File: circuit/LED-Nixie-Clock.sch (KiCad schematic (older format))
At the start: 37 parts, among them J1 USB Micro, J2 Debug, J3 Serial, SW1 Boot0, U1 MCP1700-3302E_SOT23, U2 STM32F103C8Tx, Y1 8MHz, Y2 32.768kHz

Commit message: Reroute PCB traces for more compact layout and 5032 crystal
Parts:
- Y1: footprint Crystal:Crystal_SMD_HC49-SD -> Crystal:Crystal_SMD_5032-2Pin_5.0x3.2mm
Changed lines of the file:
@@
 F 0 "Y1" V 1554 3981 50  0000 L CNN
 F 1 "8MHz" V 1645 3981 50  0000 L CNN
-F 2 "Crystal:Crystal_SMD_HC49-SD" H 1600 3850 50  0001 C CNN
+F 2 "Crystal:Crystal_SMD_5032-2Pin_5.0x3.2mm" H 1600 3850 50  0001 C CNN
 F 3 "~" H 1600 3850 50  0001 C CNN
 	1    1600 3850

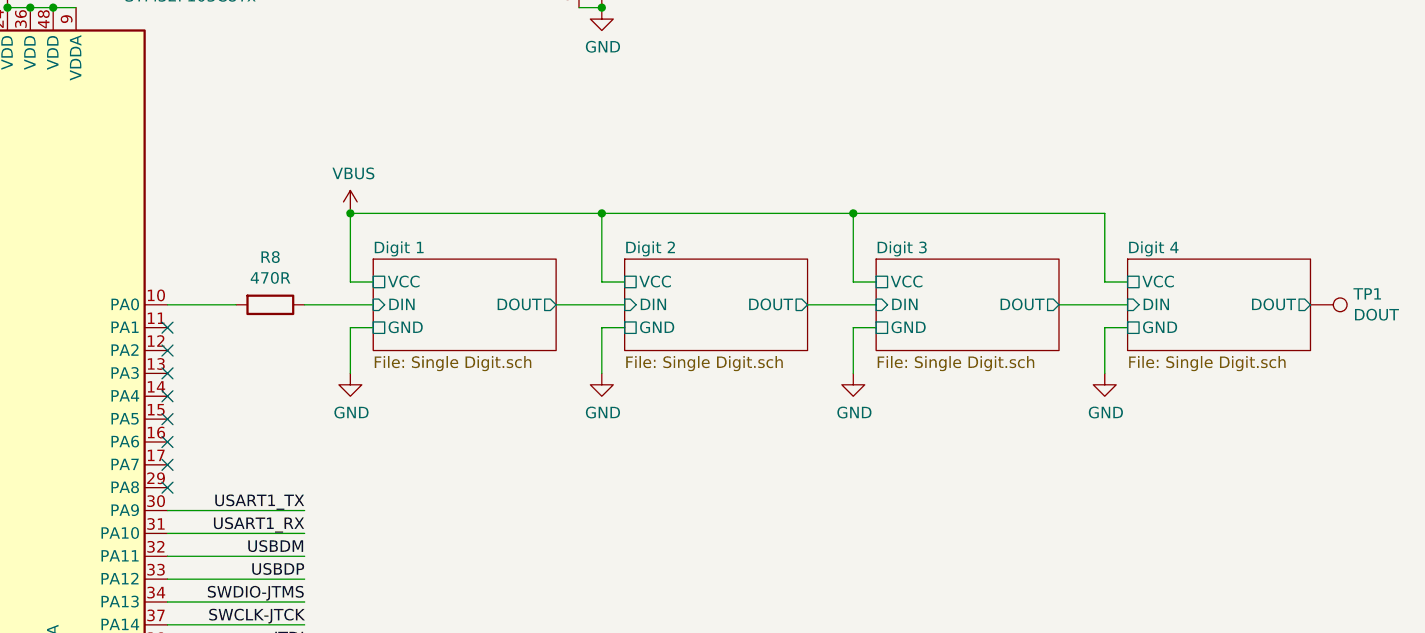
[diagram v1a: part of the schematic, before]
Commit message: Move LED data bus to PA2 (which is on the same pin as USART2 Tx)
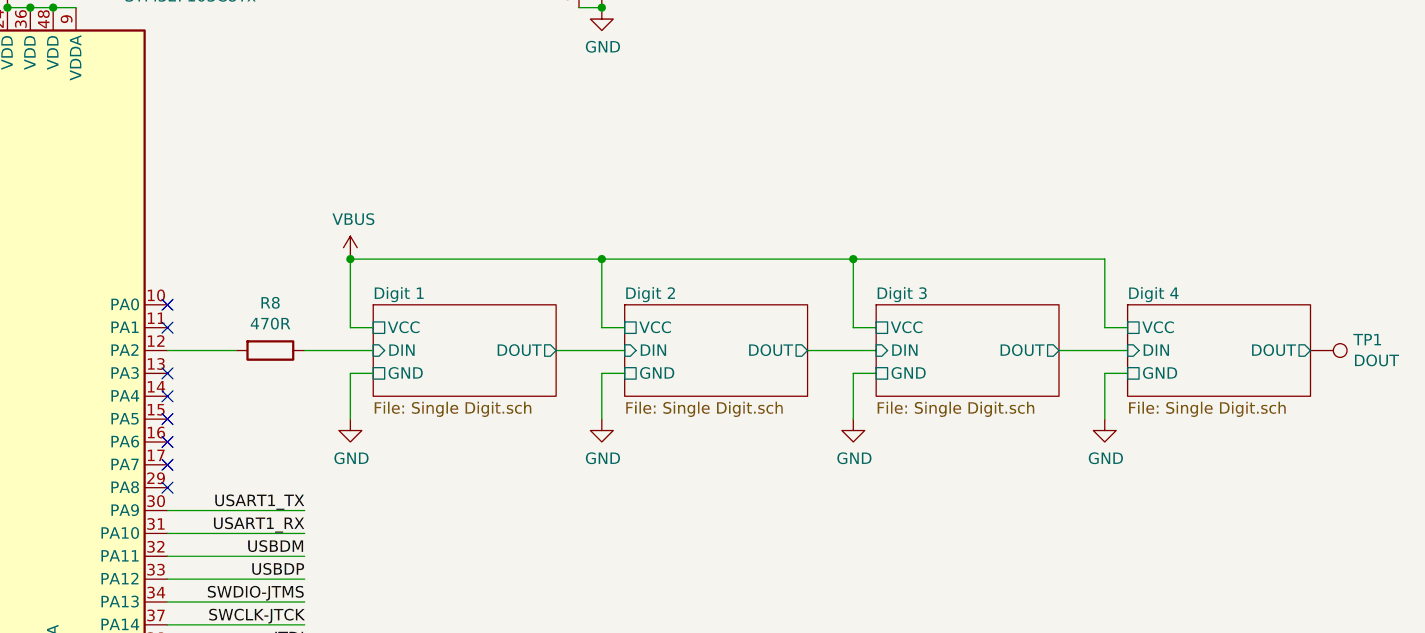
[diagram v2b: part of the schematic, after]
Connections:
- net at U2.10 (PA0): no longer R8.2
- net at U2.12 (PA2): now also R8.2
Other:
- moved on the sheet: R8, TP1
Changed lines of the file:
@@
 $EndComp
 $Sheet
-S 6400 3300 800  400
+S 6400 3500 800  400
 U 5C39F816
 F0 "Digit 1" 50
 F1 "Single Digit.sch" 50
-F2 "VCC" U L 6400 3400 50
-F3 "GND" U L 6400 3600 50
-F4 "DIN" I L 6400 3500 50
-F5 "DOUT" O R 7200 3500 50
+F2 "VCC" U L 6400 3600 50
+F3 "GND" U L 6400 3800 50
+F4 "DIN" I L 6400 3700 50
+F5 "DOUT" O R 7200 3700 50
 $EndSheet
 $Comp
@@
 NoConn ~ 5500 3900
 NoConn ~ 5500 3800
-NoConn ~ 5500 3700
 NoConn ~ 5500 3600
 $Comp
 L Device:R R8
 U 1 1 5C3A0157
-P 5950 3500
-F 0 "R8" V 5743 3500 50  0000 C CNN
-F 1 "470R" V 5834 3500 50  0000 C CNN
-F 2 "Resistor_SMD:R_0805_2012Metric_Pad1.15x1.40mm_HandSolder" V 5880 3500 50  0001 C CNN
-F 3 "~" H 5950 3500 50  0001 C CNN
-	1    5950 3500
-	0    1    1    0
-$EndComp
-Wire Wire Line
-	5800 3500 5500 3500
+P 5950 3700
+F 0 "R8" V 5743 3700 50  0000 C CNN
+F 1 "470R" V 5834 3700 50  0000 C CNN
+F 2 "Resistor_SMD:R_0805_2012Metric_Pad1.15x1.40mm_HandSolder" V 5880 3700 50  0001 C CNN
+F 3 "~" H 5950 3700 50  0001 C CNN
+	1    5950 3700
+	0    1    1    0
+$EndComp
+Wire Wire Line
+	5800 3700 5500 3700
 $Comp
 L power:VDD #PWR0110
@@
 $EndComp
 Wire Wire Line
-	6100 3500 6400 3500
+	6100 3700 6400 3700
 $Comp
 L power:GND #PWR0113
 U 1 1 5C3A1838
-P 6300 3800
-F 0 "#PWR0113" H 6300 3550 50  0001 C CNN
-F 1 "GND" H 6305 3627 50  0000 C CNN
-F 2 "" H 6300 3800 50  0001 C CNN
-F 3 "" H 6300 3800 50  0001 C CNN
-	1    6300 3800
-	1    0    0    -1
-$EndComp
-Wire Wire Line
-	6300 3100 6300 3400
-Wire Wire Line
-	6300 3400 6400 3400
-Wire Wire Line
-	6400 3600 6300 3600
-Wire Wire Line
-	6300 3600 6300 3800
+P 6300 4000
+F 0 "#PWR0113" H 6300 3750 50  0001 C CNN
+F 1 "GND" H 6305 3827 50  0000 C CNN
+F 2 "" H 6300 4000 50  0001 C CNN
+F 3 "" H 6300 4000 50  0001 C CNN
+	1    6300 4000
+	1    0    0    -1
+$EndComp
+Wire Wire Line
+	6300 3300 6300 3600
+Wire Wire Line
+	6300 3600 6400 3600
+Wire Wire Line
+	6400 3800 6300 3800
+Wire Wire Line
+	6300 3800 6300 4000
 $Comp
 L power:VDD #PWR0157
@@
 	3600 2400 4200 2400
 $Sheet
-S 7500 3300 800  400
+S 7500 3500 800  400
 U 5C3FE993
 F0 "Digit 2" 50
 F1 "Single Digit.sch" 50
-F2 "VCC" U L 7500 3400 50
-F3 "GND" U L 7500 3600 50
-F4 "DIN" I L 7500 3500 50
-F5 "DOUT" O R 8300 3500 50
+F2 "VCC" U L 7500 3600 50
+F3 "GND" U L 7500 3800 50
+F4 "DIN" I L 7500 3700 50
+F5 "DOUT" O R 8300 3700 50
 $EndSheet
 $Comp
 L power:GND #PWR0168
 U 1 1 5C3FF583
-P 7400 3800
-F 0 "#PWR0168" H 7400 3550 50  0001 C CNN
-F 1 "GND" H 7405 3627 50  0000 C CNN
-F 2 "" H 7400 3800 50  0001 C CNN
-F 3 "" H 7400 3800 50  0001 C CNN
-	1    7400 3800
-	1    0    0    -1
-$EndComp
-Wire Wire Line
-	7400 3100 7400 3400
-Wire Wire Line
-	7400 3400 7500 3400
-Wire Wire Line
-	7500 3600 7400 3600
-Wire Wire Line
-	7400 3600 7400 3800
-Wire Wire Line
-	7200 3500 7500 3500
+P 7400 4000
+F 0 "#PWR0168" H 7400 3750 50  0001 C CNN
+F 1 "GND" H 7405 3827 50  0000 C CNN
+F 2 "" H 7400 4000 50  0001 C CNN
+F 3 "" H 7400 4000 50  0001 C CNN
+	1    7400 4000
+	1    0    0    -1
+$EndComp
+Wire Wire Line
+	7400 3300 7400 3600
+Wire Wire Line
+	7400 3600 7500 3600
+Wire Wire Line
+	7500 3800 7400 3800
+Wire Wire Line
+	7400 3800 7400 4000
+Wire Wire Line
+	7200 3700 7500 3700
 $Sheet
-S 8600 3300 800  400
+S 8600 3500 800  400
 U 5C402CAE
 F0 "Digit 3" 50
 F1 "Single Digit.sch" 50
-F2 "VCC" U L 8600 3400 50
-F3 "GND" U L 8600 3600 50
-F4 "DIN" I L 8600 3500 50
-F5 "DOUT" O R 9400 3500 50
+F2 "VCC" U L 8600 3600 50
+F3 "GND" U L 8600 3800 50
+F4 "DIN" I L 8600 3700 50
+F5 "DOUT" O R 9400 3700 50
 $EndSheet
 $Comp
 L power:GND #PWR02
 U 1 1 5C402CBB
-P 8500 3800
-F 0 "#PWR02" H 8500 3550 50  0001 C CNN
-F 1 "GND" H 8505 3627 50  0000 C CNN
-F 2 "" H 8500 3800 50  0001 C CNN
-F 3 "" H 8500 3800 50  0001 C CNN
-	1    8500 3800
-	1    0    0    -1
-$EndComp
-Wire Wire Line
-	8500 3100 8500 3400
-Wire Wire Line
-	8500 3400 8600 3400
-Wire Wire Line
-	8600 3600 8500 3600
-Wire Wire Line
-	8500 3600 8500 3800
+P 8500 4000
+F 0 "#PWR02" H 8500 3750 50  0001 C CNN
+F 1 "GND" H 8505 3827 50  0000 C CNN
+F 2 "" H 8500 4000 50  0001 C CNN
+F 3 "" H 8500 4000 50  0001 C CNN
+	1    8500 4000
+	1    0    0    -1
+$EndComp
+Wire Wire Line
+	8500 3300 8500 3600
+Wire Wire Line
+	8500 3600 8600 3600
+Wire Wire Line
+	8600 3800 8500 3800
+Wire Wire Line
+	8500 3800 8500 4000
 $Sheet
-S 9700 3300 800  400
+S 9700 3500 800  400
 U 5C402CC5
 F0 "Digit 4" 50
 F1 "Single Digit.sch" 50
-F2 "VCC" U L 9700 3400 50
-F3 "GND" U L 9700 3600 50
-F4 "DIN" I L 9700 3500 50
-F5 "DOUT" O R 10500 3500 50
+F2 "VCC" U L 9700 3600 50
+F3 "GND" U L 9700 3800 50
+F4 "DIN" I L 9700 3700 50
+F5 "DOUT" O R 10500 3700 50
 $EndSheet
 $Comp
 L power:GND #PWR04
 U 1 1 5C402CD2
-P 9600 3800
-F 0 "#PWR04" H 9600 3550 50  0001 C CNN
-F 1 "GND" H 9605 3627 50  0000 C CNN
-F 2 "" H 9600 3800 50  0001 C CNN
-F 3 "" H 9600 3800 50  0001 C CNN
-	1    9600 3800
-	1    0    0    -1
-$EndComp
-Wire Wire Line
-	9600 3400 9700 3400
-Wire Wire Line
-	9700 3600 9600 3600
-Wire Wire Line
-	9600 3600 9600 3800
-Wire Wire Line
-	9400 3500 9700 3500
-Wire Wire Line
-	8300 3500 8600 3500
+P 9600 4000
+F 0 "#PWR04" H 9600 3750 50  0001 C CNN
+F 1 "GND" H 9605 3827 50  0000 C CNN
+F 2 "" H 9600 4000 50  0001 C CNN
+F 3 "" H 9600 4000 50  0001 C CNN
+	1    9600 4000
+	1    0    0    -1
+$EndComp
+Wire Wire Line
+	9600 3600 9700 3600
+Wire Wire Line
+	9700 3800 9600 3800
+Wire Wire Line
+	9600 3800 9600 4000
+Wire Wire Line
+	9400 3700 9700 3700
+Wire Wire Line
+	8300 3700 8600 3700
 $Comp
 L Switch:SW_Push SW1
@@
 $EndComp
 Wire Wire Line
-	6300 3100 7400 3100
-Wire Wire Line
-	9600 3100 9600 3400
-Connection ~ 8500 3100
-Wire Wire Line
-	8500 3100 9600 3100
-Connection ~ 7400 3100
-Wire Wire Line
-	7400 3100 8500 3100
+	6300 3300 7400 3300
+Wire Wire Line
+	9600 3300 9600 3600
+Connection ~ 8500 3300
+Wire Wire Line
+	8500 3300 9600 3300
+Connection ~ 7400 3300
+Wire Wire Line
+	7400 3300 8500 3300
 Connection ~ 4800 2200
 Wire Wire Line
@@
 L power:VBUS #PWR0112
 U 1 1 5C5B244A
-P 6300 3100
-F 0 "#PWR0112" H 6300 2950 50  0001 C CNN
-F 1 "VBUS" H 6315 3273 50  0000 C CNN
-F 2 "" H 6300 3100 50  0001 C CNN
-F 3 "" H 6300 3100 50  0001 C CNN
-	1    6300 3100
-	1    0    0    -1
-$EndComp
-Connection ~ 6300 3100
+P 6300 3300
+F 0 "#PWR0112" H 6300 3150 50  0001 C CNN
+F 1 "VBUS" H 6315 3473 50  0000 C CNN
+F 2 "" H 6300 3300 50  0001 C CNN
+F 3 "" H 6300 3300 50  0001 C CNN
+	1    6300 3300
+	1    0    0    -1
+$EndComp
+Connection ~ 6300 3300
 Wire Wire Line
 	2900 900  2900 1100
@@
 L Connector:TestPoint TP1
 U 1 1 5C8AE386
-P 10500 3500
-F 0 "TP1" V 10454 3688 50  0000 L CNN
-F 1 "DOUT" V 10545 3688 50  0000 L CNN
-F 2 "TestPoint:TestPoint_Pad_1.0x1.0mm" H 10700 3500 50  0001 C CNN
-F 3 "~" H 10700 3500 50  0001 C CNN
-	1    10500 3500
+P 10500 3700
+F 0 "TP1" V 10454 3888 50  0000 L CNN
+F 1 "DOUT" V 10545 3888 50  0000 L CNN
+F 2 "TestPoint:TestPoint_Pad_1.0x1.0mm" H 10700 3700 50  0001 C CNN
+F 3 "~" H 10700 3700 50  0001 C CNN
+	1    10500 3700
 	0    1    1    0
 $EndComp
@@
 Wire Wire Line
 	2400 6400 2800 6400
+NoConn ~ 5500 3500
 $EndSCHEMATC

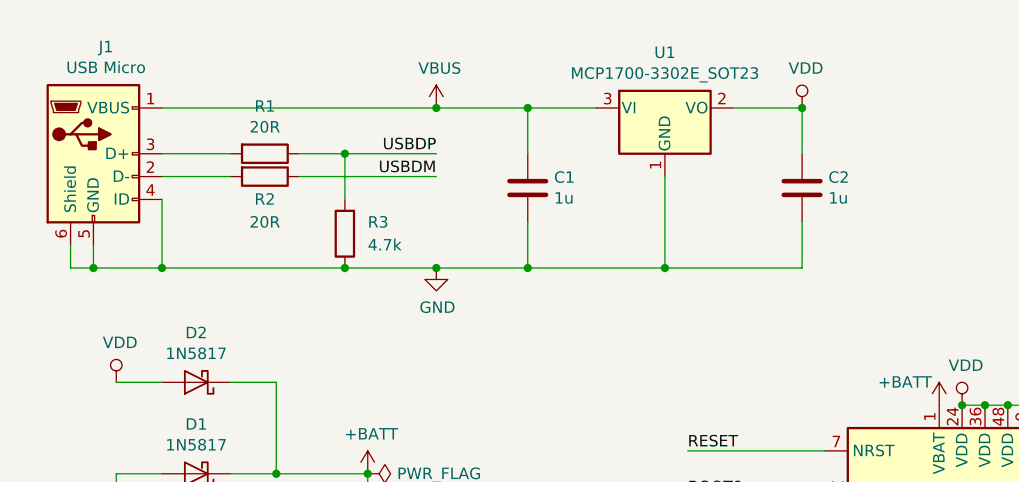
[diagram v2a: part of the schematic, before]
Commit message: Fix USBDP pull up resistor
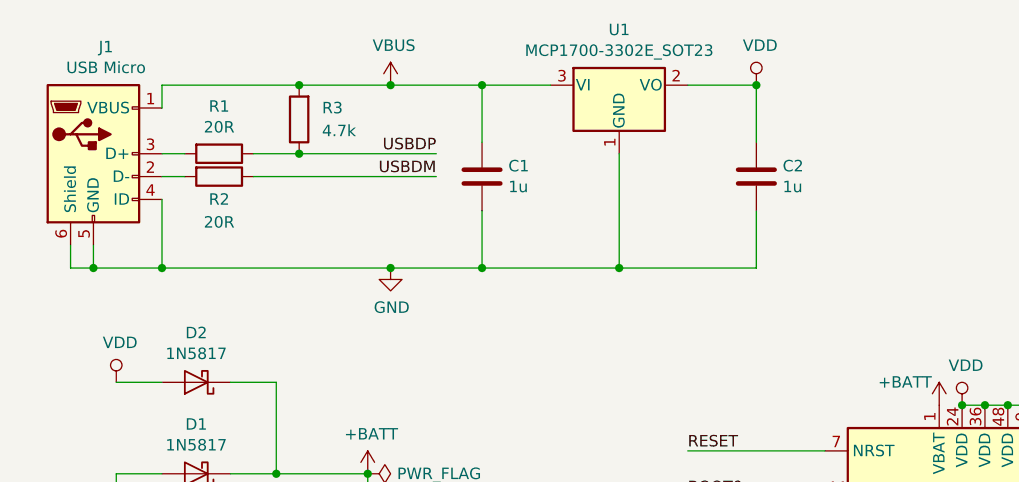
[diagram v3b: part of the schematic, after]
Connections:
- net GND: no longer R3.1
- net USBDP: now also R3.1; no longer R3.2
- net VBUS: now also R3.2
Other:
- moved on the sheet: C1, C2, R1, R2, R3, U1
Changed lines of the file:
@@
 L power:VDD #PWR0110
 U 1 1 5C3A07BC
-P 4100 900
-F 0 "#PWR0110" H 4100 750 50  0001 C CNN
-F 1 "VDD" H 4117 1073 50  0000 C CNN
-F 2 "" H 4100 900 50  0001 C CNN
-F 3 "" H 4100 900 50  0001 C CNN
-	1    4100 900
+P 3900 800
+F 0 "#PWR0110" H 3900 650 50  0001 C CNN
+F 1 "VDD" H 3917 973 50  0000 C CNN
+F 2 "" H 3900 800 50  0001 C CNN
+F 3 "" H 3900 800 50  0001 C CNN
+	1    3900 800
 	1    0    0    -1
 $EndComp
@@
 L Device:C C2
 U 1 1 5C424CF6
-P 4100 1250
-F 0 "C2" H 4215 1296 50  0000 L CNN
-F 1 "1u" H 4215 1205 50  0000 L CNN
-F 2 "Capacitor_SMD:C_0805_2012Metric_Pad1.15x1.40mm_HandSolder" H 4138 1100 50  0001 C CNN
-F 3 "~" H 4100 1250 50  0001 C CNN
-	1    4100 1250
+P 3900 1200
+F 0 "C2" H 4015 1246 50  0000 L CNN
+F 1 "1u" H 4015 1155 50  0000 L CNN
+F 2 "Capacitor_SMD:C_0805_2012Metric_Pad1.15x1.40mm_HandSolder" H 3938 1050 50  0001 C CNN
+F 3 "~" H 3900 1200 50  0001 C CNN
+	1    3900 1200
 	1    0    0    -1
 $EndComp
@@
 L Device:C C1
 U 1 1 5C4296AB
-P 2900 1250
-F 0 "C1" H 3015 1296 50  0000 L CNN
-F 1 "1u" H 3015 1205 50  0000 L CNN
-F 2 "Capacitor_SMD:C_0805_2012Metric_Pad1.15x1.40mm_HandSolder" H 2938 1100 50  0001 C CNN
-F 3 "~" H 2900 1250 50  0001 C CNN
-	1    2900 1250
+P 2700 1200
+F 0 "C1" H 2815 1246 50  0000 L CNN
+F 1 "1u" H 2815 1155 50  0000 L CNN
+F 2 "Capacitor_SMD:C_0805_2012Metric_Pad1.15x1.40mm_HandSolder" H 2738 1050 50  0001 C CNN
+F 3 "~" H 2700 1200 50  0001 C CNN
+	1    2700 1200
 	1    0    0    -1
 $EndComp
@@
 L Device:R R1
 U 1 1 5C5376C5
-P 1750 1100
-F 0 "R1" V 1543 1100 50  0000 C CNN
-F 1 "20R" V 1634 1100 50  0000 C CNN
-F 2 "Resistor_SMD:R_0805_2012Metric_Pad1.15x1.40mm_HandSolder" V 1680 1100 50  0001 C CNN
-F 3 "~" H 1750 1100 50  0001 C CNN
-	1    1750 1100
+P 1550 1100
+F 0 "R1" V 1343 1100 50  0000 C CNN
+F 1 "20R" V 1434 1100 50  0000 C CNN
+F 2 "Resistor_SMD:R_0805_2012Metric_Pad1.15x1.40mm_HandSolder" V 1480 1100 50  0001 C CNN
+F 3 "~" H 1550 1100 50  0001 C CNN
+	1    1550 1100
 	0    1    1    0
 $EndComp
@@
 L Device:R R2
 U 1 1 5C537844
-P 1750 1200
-F 0 "R2" V 1850 1200 50  0000 C CNN
-F 1 "20R" V 1950 1200 50  0000 C CNN
-F 2 "Resistor_SMD:R_0805_2012Metric_Pad1.15x1.40mm_HandSolder" V 1680 1200 50  0001 C CNN
-F 3 "~" H 1750 1200 50  0001 C CNN
-	1    1750 1200
+P 1550 1200
+F 0 "R2" V 1650 1200 50  0000 C CNN
+F 1 "20R" V 1750 1200 50  0000 C CNN
+F 2 "Resistor_SMD:R_0805_2012Metric_Pad1.15x1.40mm_HandSolder" V 1480 1200 50  0001 C CNN
+F 3 "~" H 1550 1200 50  0001 C CNN
+	1    1550 1200
 	0    1    1    0
 $EndComp
@@
 L Device:R R3
 U 1 1 5C537960
-P 2100 1450
-F 0 "R3" H 2000 1400 50  0000 R CNN
-F 1 "4.7k" H 2000 1500 50  0000 R CNN
-F 2 "Resistor_SMD:R_0805_2012Metric_Pad1.15x1.40mm_HandSolder" V 2030 1450 50  0001 C CNN
-F 3 "~" H 2100 1450 50  0001 C CNN
-	1    2100 1450
+P 1900 950
+F 0 "R3" H 1800 900 50  0000 R CNN
+F 1 "4.7k" H 1800 1000 50  0000 R CNN
+F 2 "Resistor_SMD:R_0805_2012Metric_Pad1.15x1.40mm_HandSolder" V 1830 950 50  0001 C CNN
+F 3 "~" H 1900 950 50  0001 C CNN
+	1    1900 950
 	-1   0    0    1
 $EndComp
@@
 L power:GND #PWR0155
 U 1 1 5C537BA3
-P 2500 1600
-F 0 "#PWR0155" H 2500 1350 50  0001 C CNN
-F 1 "GND" H 2505 1427 50  0000 C CNN
-F 2 "" H 2500 1600 50  0001 C CNN
-F 3 "" H 2500 1600 50  0001 C CNN
-	1    2500 1600
-	1    0    0    -1
-$EndComp
-Wire Wire Line
-	1300 1100 1600 1100
-Wire Wire Line
-	1300 1200 1600 1200
+P 2300 1600
+F 0 "#PWR0155" H 2300 1350 50  0001 C CNN
+F 1 "GND" H 2305 1427 50  0000 C CNN
+F 2 "" H 2300 1600 50  0001 C CNN
+F 3 "" H 2300 1600 50  0001 C CNN
+	1    2300 1600
+	1    0    0    -1
+$EndComp
 Wire Wire Line
 	1300 1300 1300 1600
 Wire Wire Line
-	1900 1200 2500 1200
-Wire Wire Line
-	1900 1100 2100 1100
-Wire Wire Line
-	2100 1100 2100 1300
-Connection ~ 2100 1100
-Wire Wire Line
-	2100 1100 2500 1100
+	1700 1200 2500 1200
+Wire Wire Line
+	1700 1100 1900 1100
+Connection ~ 1900 1100
+Wire Wire Line
+	1900 1100 2500 1100
 Wire Wire Line
 	5500 4600 6100 4600
@@
 Connection ~ 1100 4100
 Wire Wire Line
-	1000 1600 1300 1600
-Wire Wire Line
 	900  1500 900  1600
 Wire Wire Line
 	900  1600 1000 1600
-Connection ~ 1000 1600
 Wire Wire Line
 	1000 1600 1000 1500
-Connection ~ 1300 1600
-Wire Wire Line
-	1300 1600 2100 1600
 $Comp
 L power:VBUS #PWR0111
 U 1 1 5C5A3844
-P 2500 900
-F 0 "#PWR0111" H 2500 750 50  0001 C CNN
-F 1 "VBUS" H 2515 1073 50  0000 C CNN
-F 2 "" H 2500 900 50  0001 C CNN
-F 3 "" H 2500 900 50  0001 C CNN
-	1    2500 900
+P 2300 800
+F 0 "#PWR0111" H 2300 650 50  0001 C CNN
+F 1 "VBUS" H 2315 973 50  0000 C CNN
+F 2 "" H 2300 800 50  0001 C CNN
+F 3 "" H 2300 800 50  0001 C CNN
+	1    2300 800
 	1    0    0    -1
 $EndComp
@@
 Connection ~ 6300 3300
 Wire Wire Line
-	2900 900  2900 1100
-Wire Wire Line
-	3800 900  4100 900
-Wire Wire Line
-	2900 900  3200 900
-Wire Wire Line
-	2900 1400 2900 1600
-Wire Wire Line
-	4100 1100 4100 900
-Connection ~ 4100 900
-Wire Wire Line
-	3500 1200 3500 1600
-Wire Wire Line
-	3500 1600 4100 1600
-Wire Wire Line
-	4100 1400 4100 1600
-Wire Wire Line
-	2500 900  2900 900
-Connection ~ 2900 900
-Wire Wire Line
-	2500 1600 2900 1600
-Wire Wire Line
-	2500 900  1300 900
-Connection ~ 2500 900
-Wire Wire Line
-	2100 1600 2500 1600
-Connection ~ 2100 1600
-Connection ~ 2500 1600
+	2700 800  2700 1050
+Wire Wire Line
+	3600 800  3900 800
+Wire Wire Line
+	2700 800  3000 800
+Wire Wire Line
+	2700 1350 2700 1600
+Wire Wire Line
+	3900 1050 3900 800
+Connection ~ 3900 800
+Wire Wire Line
+	3300 1100 3300 1600
+Wire Wire Line
+	3300 1600 3900 1600
+Wire Wire Line
+	3900 1350 3900 1600
+Wire Wire Line
+	2300 800  2700 800
+Connection ~ 2700 800
+Wire Wire Line
+	2300 1600 2700 1600
+Wire Wire Line
+	2300 800  1900 800
+Connection ~ 2300 800
+Connection ~ 2300 1600
 $Comp
 L power:+BATT #PWR0114
@@
 L Regulator_Linear:MCP1700-3302E_SOT23 U1
 U 1 1 5C8BC8BE
-P 3500 900
-F 0 "U1" H 3500 1142 50  0000 C CNN
-F 1 "MCP1700-3302E_SOT23" H 3500 1051 50  0000 C CNN
-F 2 "Package_TO_SOT_SMD:SOT-23_Handsoldering" H 3500 1125 50  0001 C CNN
-F 3 "http://ww1.microchip.com/downloads/en/DeviceDoc/20001826C.pdf" H 3500 900 50  0001 C CNN
-	1    3500 900
-	1    0    0    -1
-$EndComp
-Wire Wire Line
-	2900 1600 3500 1600
-Connection ~ 2900 1600
-Connection ~ 3500 1600
+P 3300 800
+F 0 "U1" H 3300 1042 50  0000 C CNN
+F 1 "MCP1700-3302E_SOT23" H 3300 951 50  0000 C CNN
+F 2 "Package_TO_SOT_SMD:SOT-23_Handsoldering" H 3300 1025 50  0001 C CNN
+F 3 "http://ww1.microchip.com/downloads/en/DeviceDoc/20001826C.pdf" H 3300 800 50  0001 C CNN
+	1    3300 800
+	1    0    0    -1
+$EndComp
+Wire Wire Line
+	2700 1600 3300 1600
+Connection ~ 2700 1600
+Connection ~ 3300 1600
 $Comp
 L Mechanical:MountingHole H6
@@
 	2400 6400 2800 6400
 NoConn ~ 5500 3500
+Connection ~ 1900 800
+Wire Wire Line
+	1300 800  1300 900
+Wire Wire Line
+	1300 800  1900 800
+Wire Wire Line
+	1300 1100 1400 1100
+Wire Wire Line
+	1300 1200 1400 1200
+Wire Wire Line
+	1300 1600 2300 1600
+Wire Wire Line
+	1000 1600 1300 1600
+Connection ~ 1000 1600
+Connection ~ 1300 1600
 $EndSCHEMATC
